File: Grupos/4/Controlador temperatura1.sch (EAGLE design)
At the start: 13 parts, among them M1 NUCLEO-L452RE, U1 MAX31855KASA+T, X1 1729128

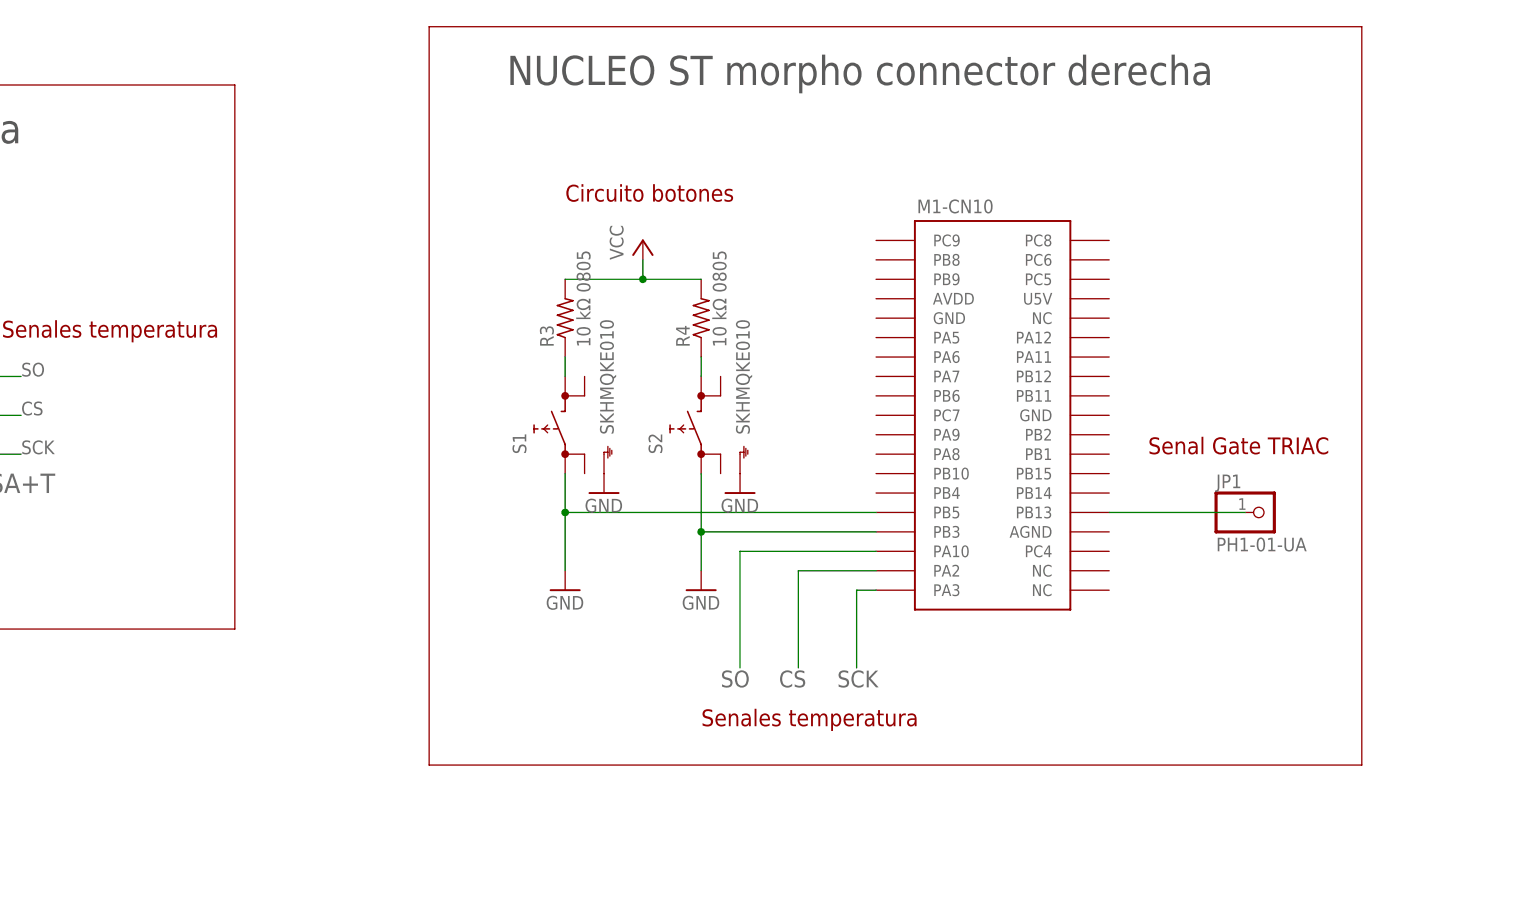
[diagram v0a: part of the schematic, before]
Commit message: Se agrea el zer-cross, se cambian señales de luar, se arregla el botón
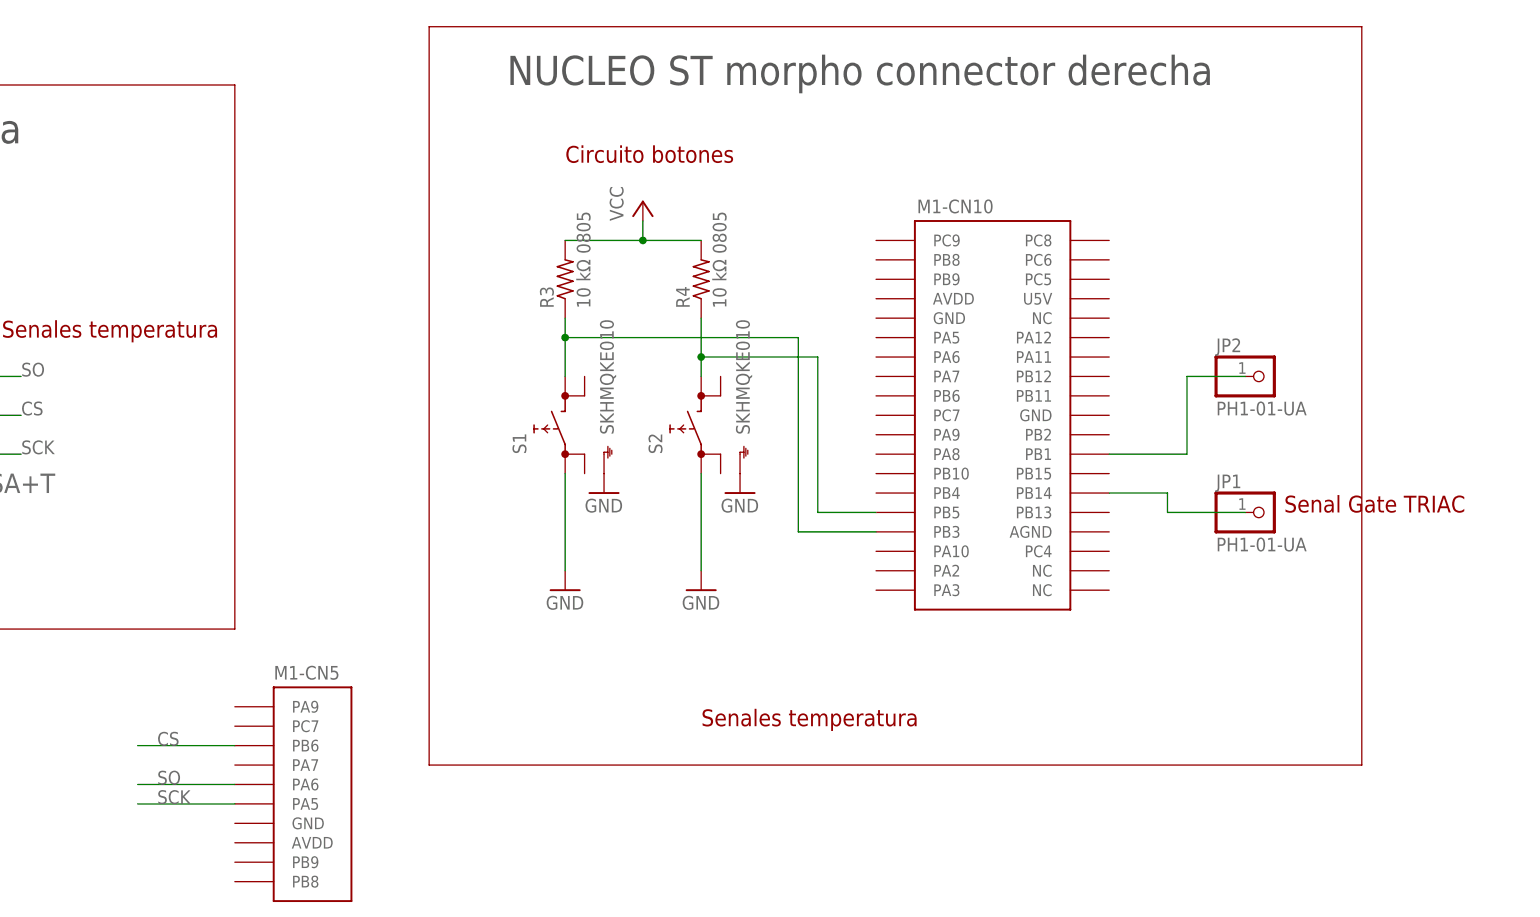
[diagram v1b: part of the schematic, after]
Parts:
- added JP2: PH1-01-UA, pinhead:PINHD-1X1
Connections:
- removed net N$12: JP1.1, M1-CN10.PB13
- new net N$3: JP1.1, M1-CN10.PB14
- new net N$4: JP2.1, M1-CN10.PB1
- net CS: now also M1-CN5.PB6; no longer M1-CN10.PA2
- net GND: no longer M1-CN10.PB3, M1-CN10.PB5
- net N$10: now also M1-CN10.PB3
- net N$11: now also M1-CN10.PB5
- net SCK: now also M1-CN5.PA5; no longer M1-CN10.PA3
- net SO: now also M1-CN5.PA6; no longer M1-CN10.PA10
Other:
- moved on the sheet: R3, R4
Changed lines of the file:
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@@
 <drawing>
 <settings>
-<setting alwaysvectorfont="no"/>
+<setting alwaysvectorfont="yes"/>
 <setting verticaltext="up"/>
 </settings>
@@
 <part name="GND8" library="supply1" library_urn="urn:adsk.eagle:library:371" deviceset="GND" device=""/>
 <part name="GND9" library="supply1" library_urn="urn:adsk.eagle:library:371" deviceset="GND" device=""/>
+<part name="JP2" library="pinhead" library_urn="urn:adsk.eagle:library:325" deviceset="PINHD-1X1" device="" package3d_urn="urn:adsk.eagle:package:22485/2" value="PH1-01-UA">
+<attribute name="PARTNO" value="PH1-01-UA"/>
+</part>
 </parts>
 <sheets>
@@
 <text x="-109.22" y="142.24" size="3.81" layer="97">NUCLEO ST morpho connector izquierda</text>
 <text x="22.86" y="50.8" size="3.81" layer="97">NUCLEO ST morpho connector derecha</text>
-<text x="30.48" y="35.56" size="2.1844" layer="94">Circuito botones</text>
+<text x="30.48" y="40.64" size="2.1844" layer="94">Circuito botones</text>
 <text x="48.26" y="-33.02" size="2.1844" layer="94">Senales temperatura</text>
-<text x="106.68" y="2.54" size="2.1844" layer="94">Senal Gate TRIAC</text>
+<text x="124.46" y="-5.08" size="2.1844" layer="94">Senal Gate TRIAC</text>
 <text x="-101.6" y="109.22" size="2.1844" layer="94">Circuito LEDs</text>
 <text x="-38.1" y="116.84" size="2.1844" layer="94">Power</text>
@@
 <attribute name="PARTNO" x="48.26" y="5.08" size="2.1844" layer="96" rot="R90" display="off"/>
 </instance>
-<instance part="R3" gate="G$1" x="30.48" y="20.32" smashed="yes" rot="R90">
-<attribute name="NAME" x="28.9814" y="16.51" size="1.778" layer="95" rot="R90"/>
-<attribute name="VALUE" x="33.782" y="16.51" size="1.778" layer="96" rot="R90"/>
-<attribute name="PARTNO" x="30.48" y="20.32" size="2.1844" layer="96" rot="R90" display="off"/>
-</instance>
-<instance part="R4" gate="G$1" x="48.26" y="20.32" smashed="yes" rot="R90">
-<attribute name="NAME" x="46.7614" y="16.51" size="1.778" layer="95" rot="R90"/>
-<attribute name="VALUE" x="51.562" y="16.51" size="1.778" layer="96" rot="R90"/>
-<attribute name="PARTNO" x="48.26" y="20.32" size="2.1844" layer="96" rot="R90" display="off"/>
+<instance part="R3" gate="G$1" x="30.48" y="25.4" smashed="yes" rot="R90">
+<attribute name="NAME" x="28.9814" y="21.59" size="1.778" layer="95" rot="R90"/>
+<attribute name="VALUE" x="33.782" y="21.59" size="1.778" layer="96" rot="R90"/>
+<attribute name="PARTNO" x="30.48" y="25.4" size="2.1844" layer="96" rot="R90" display="off"/>
+</instance>
+<instance part="R4" gate="G$1" x="48.26" y="25.4" smashed="yes" rot="R90">
+<attribute name="NAME" x="46.7614" y="21.59" size="1.778" layer="95" rot="R90"/>
+<attribute name="VALUE" x="51.562" y="21.59" size="1.778" layer="96" rot="R90"/>
+<attribute name="PARTNO" x="48.26" y="25.4" size="2.1844" layer="96" rot="R90" display="off"/>
 </instance>
 <instance part="GND5" gate="1" x="30.48" y="-15.24" smashed="yes">
@@
 <attribute name="PARTNO" x="-73.66" y="17.78" size="3.81" layer="96" display="off"/>
 </instance>
-<instance part="P+3" gate="VCC" x="40.64" y="30.48" smashed="yes">
-<attribute name="VALUE" x="38.1" y="27.94" size="1.778" layer="96" rot="R90"/>
+<instance part="P+3" gate="VCC" x="40.64" y="35.56" smashed="yes">
+<attribute name="VALUE" x="38.1" y="33.02" size="1.778" layer="96" rot="R90"/>
 </instance>
 <instance part="GND8" gate="1" x="53.34" y="-2.54" smashed="yes">
@@
 <instance part="GND9" gate="1" x="35.56" y="-2.54" smashed="yes">
 <attribute name="VALUE" x="33.02" y="-5.08" size="1.778" layer="96"/>
+</instance>
+<instance part="JP2" gate="G$1" x="121.92" y="12.7" smashed="yes">
+<attribute name="NAME" x="115.57" y="15.875" size="1.778" layer="95"/>
+<attribute name="VALUE" x="115.57" y="7.62" size="1.778" layer="96"/>
+<attribute name="PARTNO" x="121.92" y="12.7" size="2.1844" layer="96" display="off"/>
+</instance>
+<instance part="M1" gate="-CN5" x="-5.08" y="-43.18" smashed="yes">
+<attribute name="NAME" x="-7.62" y="-26.924" size="1.778" layer="95"/>
 </instance>
 </instances>
@@
 <pinref part="GND5" gate="1" pin="GND"/>
 <pinref part="S1" gate="G$1" pin="1.1"/>
-<wire x1="30.48" y1="0" x2="30.48" y2="-5.08" width="0.1524" layer="91"/>
-<pinref part="M1" gate="-CN10" pin="PB5"/>
-<wire x1="30.48" y1="-5.08" x2="30.48" y2="-12.7" width="0.1524" layer="91"/>
-<wire x1="71.12" y1="-5.08" x2="30.48" y2="-5.08" width="0.1524" layer="91"/>
-<junction x="30.48" y="-5.08"/>
+<wire x1="30.48" y1="0" x2="30.48" y2="-12.7" width="0.1524" layer="91"/>
 </segment>
 <segment>
 <pinref part="GND6" gate="1" pin="GND"/>
 <pinref part="S2" gate="G$1" pin="1.1"/>
-<wire x1="48.26" y1="0" x2="48.26" y2="-7.62" width="0.1524" layer="91"/>
-<pinref part="M1" gate="-CN10" pin="PB3"/>
-<wire x1="48.26" y1="-7.62" x2="48.26" y2="-12.7" width="0.1524" layer="91"/>
-<wire x1="71.12" y1="-7.62" x2="48.26" y2="-7.62" width="0.1524" layer="91"/>
-<junction x="48.26" y="-7.62"/>
+<wire x1="48.26" y1="0" x2="48.26" y2="-12.7" width="0.1524" layer="91"/>
 </segment>
 <segment>
@@
 <segment>
 <pinref part="P+3" gate="VCC" pin="VCC"/>
-<wire x1="40.64" y1="27.94" x2="40.64" y2="25.4" width="0.1524" layer="91"/>
+<wire x1="40.64" y1="33.02" x2="40.64" y2="30.48" width="0.1524" layer="91"/>
 <pinref part="R3" gate="G$1" pin="2"/>
-<wire x1="40.64" y1="25.4" x2="30.48" y2="25.4" width="0.1524" layer="91"/>
+<wire x1="40.64" y1="30.48" x2="30.48" y2="30.48" width="0.1524" layer="91"/>
 <pinref part="R4" gate="G$1" pin="2"/>
-<wire x1="40.64" y1="25.4" x2="48.26" y2="25.4" width="0.1524" layer="91"/>
-<junction x="40.64" y="25.4"/>
+<wire x1="40.64" y1="30.48" x2="48.26" y2="30.48" width="0.1524" layer="91"/>
+<junction x="40.64" y="30.48"/>
 </segment>
 </net>
@@
 <segment>
 <pinref part="S1" gate="G$1" pin="2.1"/>
-<wire x1="30.48" y1="15.24" x2="30.48" y2="12.7" width="0.1524" layer="91"/>
+<wire x1="30.48" y1="20.32" x2="30.48" y2="17.78" width="0.1524" layer="91"/>
 <pinref part="R3" gate="G$1" pin="1"/>
+<wire x1="30.48" y1="17.78" x2="30.48" y2="12.7" width="0.1524" layer="91"/>
+<wire x1="30.48" y1="17.78" x2="60.96" y2="17.78" width="0.1524" layer="91"/>
+<junction x="30.48" y="17.78"/>
+<wire x1="60.96" y1="17.78" x2="60.96" y2="-7.62" width="0.1524" layer="91"/>
+<pinref part="M1" gate="-CN10" pin="PB3"/>
+<wire x1="71.12" y1="-7.62" x2="60.96" y2="-7.62" width="0.1524" layer="91"/>
 </segment>
 </net>
@@
 <segment>
 <pinref part="S2" gate="G$1" pin="2.1"/>
+<wire x1="48.26" y1="20.32" x2="48.26" y2="15.24" width="0.1524" layer="91"/>
+<pinref part="R4" gate="G$1" pin="1"/>
+<pinref part="M1" gate="-CN10" pin="PB5"/>
 <wire x1="48.26" y1="15.24" x2="48.26" y2="12.7" width="0.1524" layer="91"/>
-<pinref part="R4" gate="G$1" pin="1"/>
+<wire x1="71.12" y1="-5.08" x2="63.5" y2="-5.08" width="0.1524" layer="91"/>
+<wire x1="63.5" y1="-5.08" x2="63.5" y2="15.24" width="0.1524" layer="91"/>
+<wire x1="63.5" y1="15.24" x2="48.26" y2="15.24" width="0.1524" layer="91"/>
+<junction x="48.26" y="15.24"/>
 </segment>
 </net>
@@
 </segment>
 </net>
-<net name="N$12" class="0">
-<segment>
-<pinref part="M1" gate="-CN10" pin="PB13"/>
-<pinref part="JP1" gate="G$1" pin="1"/>
-<wire x1="101.6" y1="-5.08" x2="119.38" y2="-5.08" width="0.1524" layer="91"/>
-</segment>
-</net>
 <net name="SO" class="0">
 <segment>
@@
 </segment>
 <segment>
-<pinref part="M1" gate="-CN10" pin="PA10"/>
-<wire x1="71.12" y1="-10.16" x2="53.34" y2="-10.16" width="0.1524" layer="91"/>
-<label x="50.8" y="-27.94" size="2.1844" layer="95"/>
-<wire x1="53.34" y1="-10.16" x2="53.34" y2="-25.4" width="0.1524" layer="91"/>
+<pinref part="M1" gate="-CN5" pin="PA6"/>
+<wire x1="-12.7" y1="-40.64" x2="-25.4" y2="-40.64" width="0.1524" layer="91"/>
+<label x="-22.86" y="-40.64" size="1.778" layer="95"/>
 </segment>
 </net>
@@
 </segment>
 <segment>
-<pinref part="M1" gate="-CN10" pin="PA2"/>
-<wire x1="71.12" y1="-12.7" x2="60.96" y2="-12.7" width="0.1524" layer="91"/>
-<label x="58.42" y="-27.94" size="2.1844" layer="95"/>
-<wire x1="60.96" y1="-12.7" x2="60.96" y2="-25.4" width="0.1524" layer="91"/>
+<pinref part="M1" gate="-CN5" pin="PB6"/>
+<wire x1="-12.7" y1="-35.56" x2="-25.4" y2="-35.56" width="0.1524" layer="91"/>
+<label x="-22.86" y="-35.56" size="1.778" layer="95"/>
 </segment>
 </net>
@@
 </segment>
 <segment>
-<pinref part="M1" gate="-CN10" pin="PA3"/>
-<wire x1="71.12" y1="-15.24" x2="68.58" y2="-15.24" width="0.1524" layer="91"/>
-<label x="66.04" y="-27.94" size="2.1844" layer="95"/>
-<wire x1="68.58" y1="-15.24" x2="68.58" y2="-25.4" width="0.1524" layer="91"/>
-</segment>
-</net>
+<pinref part="M1" gate="-CN5" pin="PA5"/>
+<wire x1="-12.7" y1="-43.18" x2="-25.4" y2="-43.18" width="0.1524" layer="91"/>
+<label x="-22.86" y="-43.18" size="1.778" layer="95"/>
+</segment>
+</net>
+<net name="N$3" class="0">
+<segment>
+<pinref part="JP1" gate="G$1" pin="1"/>
+<wire x1="119.38" y1="-5.08" x2="109.22" y2="-5.08" width="0.1524" layer="91"/>
+<wire x1="109.22" y1="-5.08" x2="109.22" y2="-2.54" width="0.1524" layer="91"/>
+<pinref part="M1" gate="-CN10" pin="PB14"/>
+<wire x1="109.22" y1="-2.54" x2="101.6" y2="-2.54" width="0.1524" layer="91"/>
+</segment>
+</net>
+<net name="N$4" class="0">
+<segment>
+<pinref part="M1" gate="-CN10" pin="PB1"/>
+<wire x1="101.6" y1="2.54" x2="111.76" y2="2.54" width="0.1524" layer="91"/>
+<wire x1="111.76" y1="2.54" x2="111.76" y2="12.7" width="0.1524" layer="91"/>
+<pinref part="JP2" gate="G$1" pin="1"/>
+<wire x1="111.76" y1="12.7" x2="119.38" y2="12.7" width="0.1524" layer="91"/>
+</segment>
+</net>
